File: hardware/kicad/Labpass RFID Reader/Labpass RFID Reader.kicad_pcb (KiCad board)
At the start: 2 copper layers, 74 x 74 mm, 54 parts, among them J1 Conn_01x03_Male, J2 Conn_01x04, Q1 BC517, U1 adafruit_huzzah_32, U2 LM393, U3 LM324, U4 MFRC522, Y1 27.12 MHz

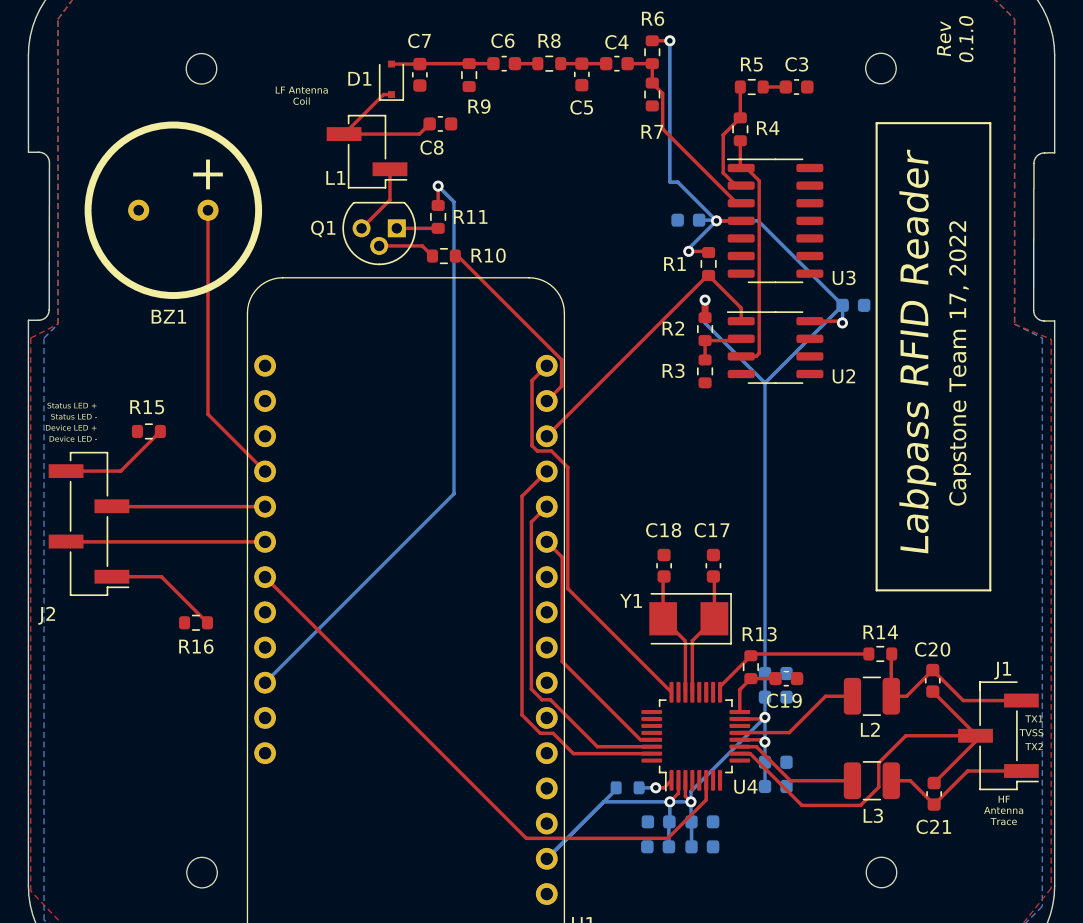
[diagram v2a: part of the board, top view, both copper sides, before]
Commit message: Add RGB LEDs with 4 wires
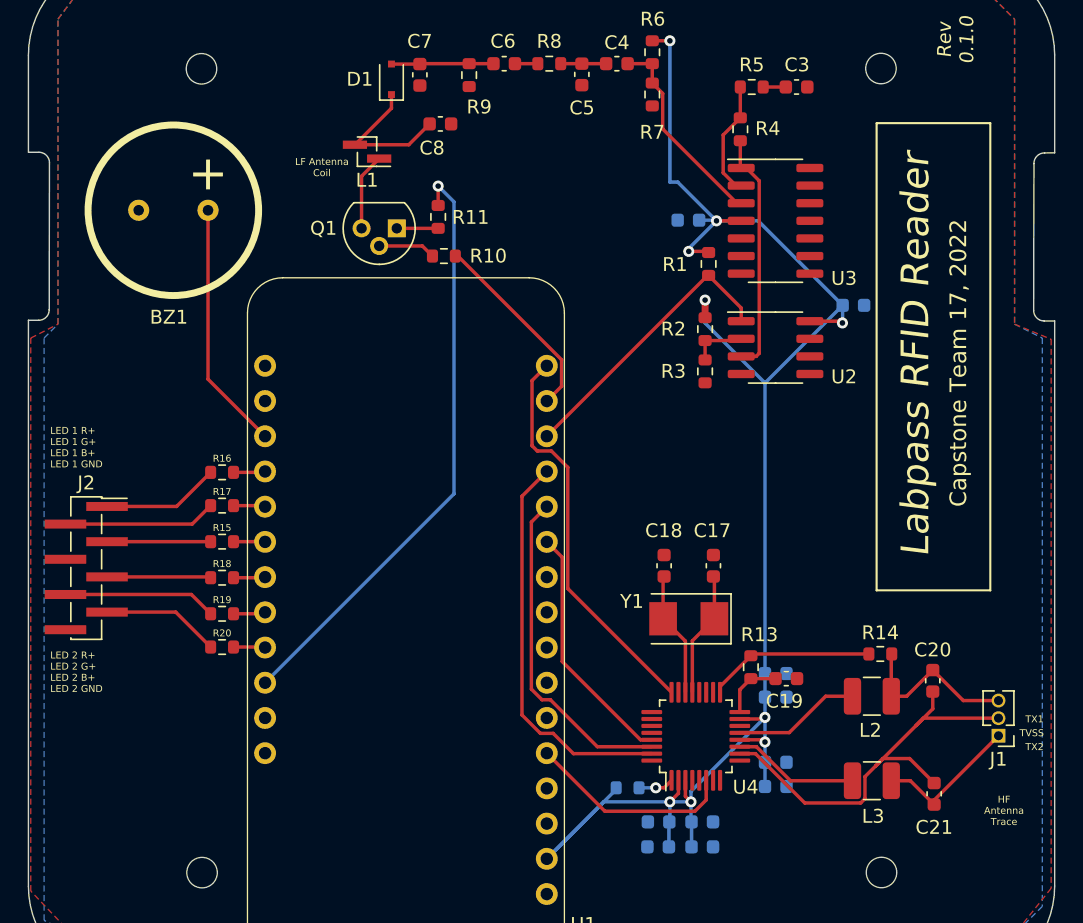
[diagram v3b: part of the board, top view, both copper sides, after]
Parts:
- added R17: R_US, Resistor_SMD:R_0603_1608Metric, F.Cu at (43.8, 70.2)
- added R18: R_US, Resistor_SMD:R_0603_1608Metric, F.Cu at (43.8, 75.4)
- added R19: R_US, Resistor_SMD:R_0603_1608Metric, F.Cu at (43.8, 78.0)
- added R20: R_US, Resistor_SMD:R_0603_1608Metric, F.Cu at (43.8, 80.4)
- J1: footprint Connector_PinHeader_2.54mm:PinHeader_1x03_P2.54mm_Vertical_SMD_Pin1Left -> Connector_PinHeader_1.27mm:PinHeader_1x03_P1.27mm_Vertical
- J2: footprint Connector_PinHeader_2.54mm:PinHeader_1x04_P2.54mm_Vertical_SMD_Pin1Left -> Connector_PinHeader_1.27mm:PinHeader_1x08_P1.27mm_Vertical_SMD_Pin1Right
- L1: footprint Connector_PinHeader_2.54mm:PinHeader_1x02_P2.54mm_Vertical_SMD_Pin1Left -> Connector_PinHeader_1.00mm:PinHeader_1x02_P1.00mm_Vertical_SMD_Pin1Left
- moved R16 11.0 mm to (43.8, 67.8)
- moved R15 9.54 mm to (43.8, 72.8)
- moved J2 3.19 mm to (34.0, 74.7), turned to 0 degrees
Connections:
- J2 pad 1: Net-(R16-Pad1) -> Net-(J2-Pad1)
- J2 pad 2: /Indicators/device_led -> Net-(J2-Pad2)
- J2 pad 3: /Indicators/status_led -> Net-(R15-Pad2)
- J2 pad 4: Net-(R15-Pad1) -> GND
- R15 pad 1: Net-(R15-Pad1) -> /Indicators/LED_1_B
- R15 pad 2: GND -> Net-(R15-Pad2)
- R16 pad 1: Net-(R16-Pad1) -> /Indicators/LED_1_R
- R16 pad 2: GND -> Net-(J2-Pad1)
- U1 pad 12: (no net) -> /Indicators/LED_2_G
- U1 pad 13: (no net) -> /Indicators/LED_2_B
- U1 pad 14: (no net) -> /Indicators/buzzer
- U1 pad 15: /Indicators/status_led -> /Indicators/LED_1_G
- U1 pad 27: /labpass_rf_13.56M/RESET -> /Indicators/LED_2_R
- U1 pad 32: /Indicators/buzzer -> /Indicators/LED_1_R
- U1 pad 33: /Indicators/device_led -> /Indicators/LED_1_B
- U1 pad A0: (no net) -> /labpass_rf_13.56M/RESET
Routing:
- net /labpass_rf_13.56M/RESET: track 42.2 -> 15.0 mm
- net /Indicators/device_led: track 14.4 -> 0.00 mm
- net /Indicators/status_led: track 11.1 -> 0.00 mm
- net Net-(J2-Pad6): track 0.00 -> 11.1 mm
- net Net-(J2-Pad2): track 0.00 -> 11.0 mm
- net Net-(J2-Pad7): track 0.00 -> 8.52 mm
- net Net-(J2-Pad1): track 0.00 -> 8.49 mm
- net Net-(R16-Pad1): track 8.26 -> 0.00 mm
- net Net-(R15-Pad1): track 7.98 -> 0.00 mm
- net Net-(J2-Pad5): track 0.00 -> 7.50 mm
- net Net-(R15-Pad2): track 0.00 -> 7.48 mm
- net /Indicators/buzzer: track 20.5 -> 18.0 mm
- net /Indicators/LED_2_G: track 0.00 -> 2.32 mm
- net /Indicators/LED_1_G: track 0.00 -> 2.31 mm
- net /Indicators/LED_1_R: track 0.00 -> 2.30 mm
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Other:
- board text added: "LED 1 R+ LED 1 G+ LED 1 B+ LED 1 GND"
- board text added: "LED 2 R+ LED 2 G+ LED 2 B+ LED 2 GND"
- board text removed: "Device LED +"
- board text removed: "Device LED -"
- board text removed: "Status LED +"
- board text removed: "Status LED -"

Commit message: last-minute fixes
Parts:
- J1: footprint Connector_PinHeader_1.27mm:PinHeader_1x03_P1.27mm_Vertical -> Connector_PinHeader_2.54mm:PinHeader_1x03_P2.54mm_Vertical_SMD_Pin1Left
- J2: footprint Connector_PinHeader_1.27mm:PinHeader_1x08_P1.27mm_Vertical_SMD_Pin1Right -> Connector_PinHeader_2.54mm:PinHeader_1x08_P2.54mm_Vertical_SMD_Pin1Right
- L1: footprint Connector_PinHeader_1.00mm:PinHeader_1x02_P1.00mm_Vertical_SMD_Pin1Left -> Connector_PinHeader_2.54mm:PinHeader_1x02_P2.54mm_Vertical_SMD_Pin1Left
- U4: footprint Package_QFP:LQFP-32_5x5mm_P0.5mm -> Package_DFN_QFN:QFN-32-1EP_5x5mm_P0.5mm_EP3.1x3.1mm
- moved J2 81.8 mm to (110.8, 102.8)
- moved J1 81.4 mm to (176.4, 114.4)
- moved C4 81.3 mm to (148.7, 65.9)
- moved R2 81.3 mm to (155.1, 85.0)
- moved R3 81.3 mm to (155.1, 88.1)
- moved R6 81.3 mm to (151.3, 65.1)
- moved R7 81.3 mm to (151.3, 68.1)
- moved BZ1 81.3 mm to (116.8, 76.5)
- moved C1 81.3 mm to (153.9, 77.2)
- moved C14 81.3 mm to (151.8, 120.6)
- moved C15 81.3 mm to (154.9, 122.4)
- moved C16 81.3 mm to (154.9, 120.6)
- moved C17 81.3 mm to (155.7, 102.1)
- moved C19 81.3 mm to (161.0, 110.2)
- moved C20 81.3 mm to (171.5, 110.4)
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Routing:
- net GND: track 0.00 -> 11.8 mm, vias 0 -> 8
- net /labpass_rf_13.56M/MISO: track 28.8 -> 32.5 mm
- net +3V3: track 126.3 -> 129.3 mm
- net Net-(C20-Pad2): track 12.5 -> 14.3 mm
- net /labpass_rf_13.56M/MOSI: track 24.0 -> 25.4 mm
- net Net-(J2-Pad7): track 8.52 -> 7.48 mm
- net Net-(J2-Pad1): track 8.49 -> 7.59 mm
- net /labpass_rf_13.56M/RX: track 12.1 -> 12.9 mm
- net /labpass_rf_13.56M/XTAL1: track 9.04 -> 9.78 mm
- net /labpass_rf_13.56M/TX1: track 9.14 -> 9.88 mm
- net /labpass_rf_13.56M/TX2: track 9.22 -> 9.96 mm
- net /labpass_rf_13.56M/SDA: track 28.8 -> 29.5 mm
- net /labpass_rf_13.56M/XTAL2: track 9.05 -> 9.79 mm
- net /labpass_rf_13.56M/SCK: track 17.9 -> 18.6 mm
- net /labpass_rf_13.56M/RESET: track 15.0 -> 15.7 mm
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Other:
- rule pad_to_mask_clearance: 0 -> 0.0508

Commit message: kicad backups
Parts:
- C19: value C -> 100n
- C20, C21: value C -> 220p
- C3: value ~ -> 100n
- J2: value Conn_01x04 -> Conn_01x08
- J3: renamed from L1; value 162u -> Conn_01x02
- L2, L3: value L -> 560n
- R13, R15, R16, R17, R18, R19, R20: value R_US -> 1k
- R14: value R_US -> 820
- R3: value 120k -> 110k
- R9: value 267k -> 222k
- U4: footprint Package_DFN_QFN:QFN-32-1EP_5x5mm_P0.5mm_EP3.1x3.1mm -> Package_QFP:LQFP-32_5x5mm_P0.5mm

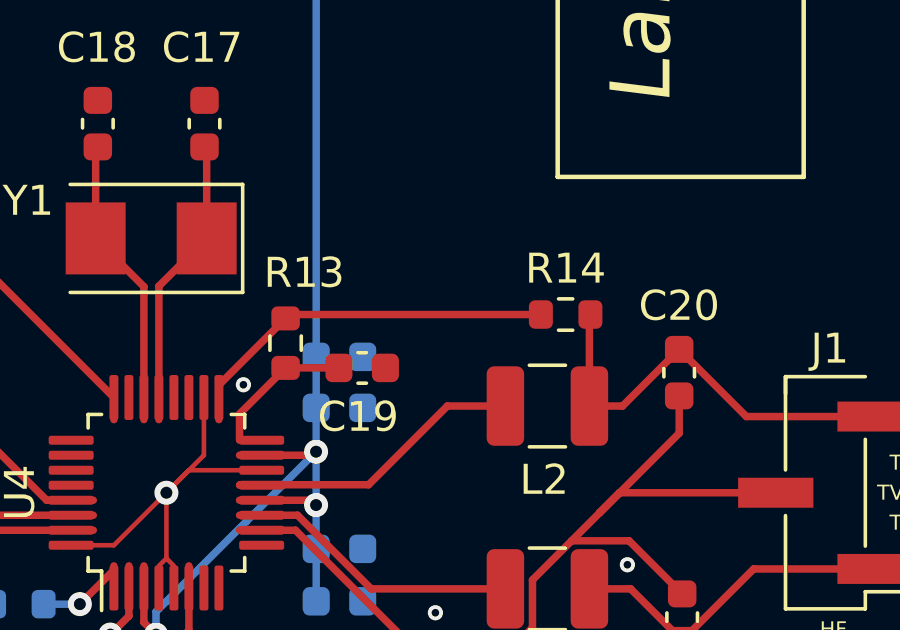
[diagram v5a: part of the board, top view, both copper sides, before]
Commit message: add missing dc blocking cap to HF path
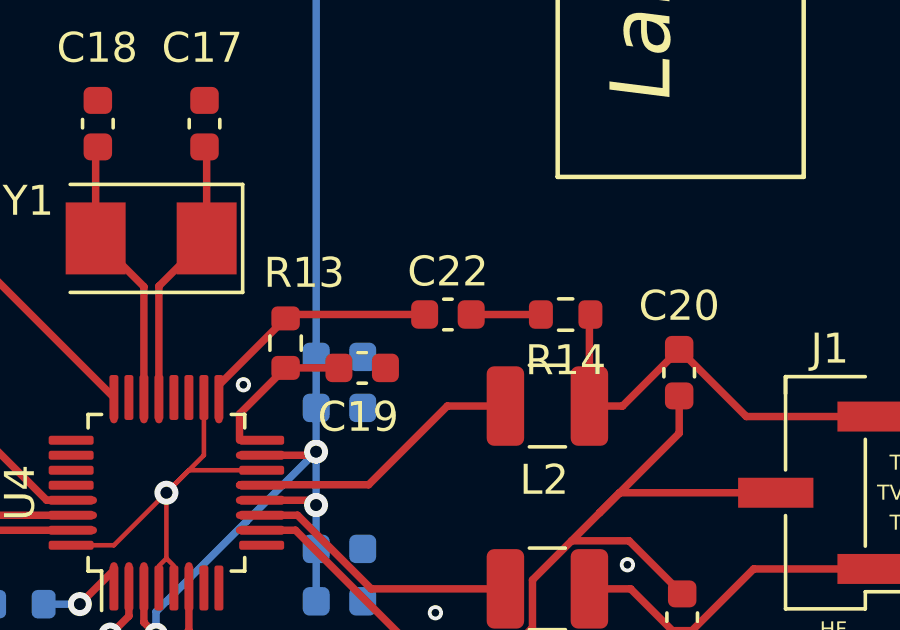
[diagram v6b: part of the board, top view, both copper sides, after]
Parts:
- added C22: 1n, Capacitor_SMD:C_0603_1608Metric, F.Cu at (163.8, 108.5)
- turned R14 to 180 degrees
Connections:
- C20 pad 2: Net-(C20-Pad2) -> Net-(R14-Pad1)
- J1 pad 3: Net-(C20-Pad2) -> Net-(R14-Pad1)
- L2 pad 2: Net-(C20-Pad2) -> Net-(R14-Pad1)
- R14 pad 1: /labpass_rf_13.56M/RX -> Net-(R14-Pad1)
- R14 pad 2: Net-(C20-Pad2) -> Net-(R14-Pad2)
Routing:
- net Net-(R14-Pad1): track 0.00 -> 14.3 mm
- net Net-(C20-Pad2): track 14.3 -> 0.00 mm
- net /labpass_rf_13.56M/RX: track 12.9 -> 8.99 mm
- net Net-(R14-Pad2): track 0.00 -> 2.33 mm
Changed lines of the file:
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@@
   (net 7 "Net-(C6-Pad2)")
   (net 8 "Net-(C8-Pad1)")
-  (net 9 "Net-(C20-Pad2)")
+  (net 9 "Net-(R14-Pad1)")
   (net 10 "Net-(C21-Pad1)")
-  (net 11 "Net-(Q1-Pad3)")
+  (net 11 "Net-(R14-Pad2)")
   (net 12 "Net-(Q1-Pad1)")
   (net 13 "Net-(Q1-Pad2)")
@@
   (net 44 "/Indicators/LED_2_B")
   (net 45 "Net-(J2-Pad3)")
+  (net 46 "Net-(J3-Pad1)")
   (footprint "Resistor_SMD:R_0603_1608Metric" (layer "F.Cu")
     (at 120.266182 100.36028 180)
@@
       (net 30 "/labpass_rf_13.56M/TX2") (pinfunction "1") (pintype "passive"))
     (pad "2" smd roundrect (at 1.4 0) (size 1.25 2.65) (layers "F.Cu" "F.Paste" "F.Mask") (roundrect_rratio 0.2)
-      (net 9 "Net-(C20-Pad2)") (pinfunction "2") (pintype "passive"))
+      (net 9 "Net-(R14-Pad1)") (pinfunction "2") (pintype "passive"))
     (model "${KICAD6_3DMODEL_DIR}/Inductor_SMD.3dshapes/L_1210_3225Metric.wrl"
       (offset (xyz 0 0 0))
@@
     (fp_line (start 1.27 -2.54) (end 1.27 2.54) (layer "F.Fab") (width 0.1))
     (pad "1" smd rect (at -1.655 -1.27 180) (size 2.51 1) (layers "F.Cu" "F.Paste" "F.Mask")
-      (net 11 "Net-(Q1-Pad3)") (pinfunction "Pin_1") (pintype "passive"))
+      (net 46 "Net-(J3-Pad1)") (pinfunction "Pin_1") (pintype "passive"))
     (pad "2" smd rect (at 1.655 1.27 180) (size 2.51 1) (layers "F.Cu" "F.Paste" "F.Mask")
       (net 8 "Net-(C8-Pad1)") (pinfunction "Pin_2") (pintype "passive"))
@@
   )
   (footprint "Resistor_SMD:R_0603_1608Metric" (layer "F.Cu")
-    (at 167.741169 108.460169)
+    (at 167.741169 108.460169 180)
     (descr "Resistor SMD 0603 (1608 Metric), square (rectangular) end terminal, IPC_7351 nominal, (Body size source: IPC-SM-782 page 72, https://www.pcb-3d.com/wordpress/wp-content/uploads/ipc-sm-782a_amendment_1_and_2.pdf), generated with kicad-footprint-generator")
     (tags "resistor")
@@
       (effects (font (size 1 1) (thickness 0.15)))
     )
-    (fp_text value "820" (at 0 -1.780169) (layer "F.Fab")
+    (fp_text value "820" (at 0 1.526169) (layer "F.Fab")
       (effects (font (size 1 1) (thickness 0.15)))
     )
@@
     (fp_line (start 0.8 -0.4125) (end 0.8 0.4125) (layer "F.Fab") (width 0.1))
     (fp_line (start -0.8 -0.4125) (end 0.8 -0.4125) (layer "F.Fab") (width 0.1))
-    (pad "1" smd roundrect (at -0.825 0) (size 0.8 0.95) (layers "F.Cu" "F.Paste" "F.Mask") (roundrect_rratio 0.25)
-      (net 32 "/labpass_rf_13.56M/RX") (pintype "passive"))
-    (pad "2" smd roundrect (at 0.825 0) (size 0.8 0.95) (layers "F.Cu" "F.Paste" "F.Mask") (roundrect_rratio 0.25)
-      (net 9 "Net-(C20-Pad2)") (pintype "passive"))
+    (pad "1" smd roundrect (at -0.825 0 180) (size 0.8 0.95) (layers "F.Cu" "F.Paste" "F.Mask") (roundrect_rratio 0.25)
+      (net 9 "Net-(R14-Pad1)") (pintype "passive"))
+    (pad "2" smd roundrect (at 0.825 0 180) (size 0.8 0.95) (layers "F.Cu" "F.Paste" "F.Mask") (roundrect_rratio 0.25)
+      (net 11 "Net-(R14-Pad2)") (pintype "passive"))
     (model "${KICAD6_3DMODEL_DIR}/Resistor_SMD.3dshapes/R_0603_1608Metric.wrl"
       (offset (xyz 0 0 0))
@@
       (net 13 "Net-(Q1-Pad2)") (pinfunction "B") (pintype "input"))
     (pad "3" thru_hole circle (at 2.54 0 180) (size 1.3 1.3) (drill 0.75) (layers *.Cu *.Mask)
-      (net 11 "Net-(Q1-Pad3)") (pinfunction "E") (pintype "passive"))
+      (net 46 "Net-(J3-Pad1)") (pinfunction "E") (pintype "passive"))
     (model "${KICAD6_3DMODEL_DIR}/Package_TO_SOT_THT.3dshapes/TO-92.wrl"
       (offset (xyz 0 0 0))
@@
       (net 29 "/labpass_rf_13.56M/TVSS") (pinfunction "Pin_2") (pintype "passive"))
     (pad "3" smd rect (at -1.655 2.54 180) (size 2.51 1) (layers "F.Cu" "F.Paste" "F.Mask")
-      (net 9 "Net-(C20-Pad2)") (pinfunction "Pin_3") (pintype "passive"))
+      (net 9 "Net-(R14-Pad1)") (pinfunction "Pin_3") (pintype "passive"))
     (model "${KICAD6_3DMODEL_DIR}/Connector_PinHeader_2.54mm.3dshapes/PinHeader_1x03_P2.54mm_Vertical_SMD_Pin1Left.wrl"
       (offset (xyz 0 0 0))
@@
       (net 29 "/labpass_rf_13.56M/TVSS") (pintype "passive"))
     (pad "2" smd roundrect (at 0.775 0 90) (size 0.9 0.95) (layers "F.Cu" "F.Paste" "F.Mask") (roundrect_rratio 0.25)
-      (net 9 "Net-(C20-Pad2)") (pintype "passive"))
+      (net 9 "Net-(R14-Pad1)") (pintype "passive"))
+    (model "${KICAD6_3DMODEL_DIR}/Capacitor_SMD.3dshapes/C_0603_1608Metric.wrl"
+      (offset (xyz 0 0 0))
+      (scale (xyz 1 1 1))
+      (rotate (xyz 0 0 0))
+    )
+  )
+  (footprint "Capacitor_SMD:C_0603_1608Metric" (layer "F.Cu")
+    (at 163.817 108.458)
+    (descr "Capacitor SMD 0603 (1608 Metric), square (rectangular) end terminal, IPC_7351 nominal, (Body size source: IPC-SM-782 page 76, https://www.pcb-3d.com/wordpress/wp-content/uploads/ipc-sm-782a_amendment_1_and_2.pdf), generated with kicad-footprint-generator")
+    (tags "capacitor")
+    (property "Sheetfile" "HF_RF.kicad_sch")
+    (property "Sheetname" "labpass_rf_13.56M")
+    (attr smd)
+    (fp_text reference "C22" (at 0 -1.43) (layer "F.SilkS")
+      (effects (font (size 1 1) (thickness 0.15)))
+    )
+    (fp_text value "1n" (at 0 1.43) (layer "F.Fab")
+      (effects (font (size 1 1) (thickness 0.15)))
+    )
+    (fp_text user "${REFERENCE}" (at 0 0) (layer "F.Fab")
+      (effects (font (size 0.4 0.4) (thickness 0.06)))
+    )
+    (fp_line (start -0.14058 0.51) (end 0.14058 0.51) (layer "F.SilkS") (width 0.12))
+    (fp_line (start -0.14058 -0.51) (end 0.14058 -0.51) (layer "F.SilkS") (width 0.12))
+    (fp_line (start -1.48 -0.73) (end 1.48 -0.73) (layer "F.CrtYd") (width 0.05))
+    (fp_line (start 1.48 -0.73) (end 1.48 0.73) (layer "F.CrtYd") (width 0.05))
+    (fp_line (start 1.48 0.73) (end -1.48 0.73) (layer "F.CrtYd") (width 0.05))
+    (fp_line (start -1.48 0.73) (end -1.48 -0.73) (layer "F.CrtYd") (width 0.05))
+    (fp_line (start -0.8 -0.4) (end 0.8 -0.4) (layer "F.Fab") (width 0.1))
+    (fp_line (start 0.8 0.4) (end -0.8 0.4) (layer "F.Fab") (width 0.1))
+    (fp_line (start 0.8 -0.4) (end 0.8 0.4) (layer "F.Fab") (width 0.1))
+    (fp_line (start -0.8 0.4) (end -0.8 -0.4) (layer "F.Fab") (width 0.1))
+    (pad "1" smd roundrect (at -0.775 0) (size 0.9 0.95) (layers "F.Cu" "F.Paste" "F.Mask") (roundrect_rratio 0.25)
+      (net 32 "/labpass_rf_13.56M/RX") (pintype "passive"))
+    (pad "2" smd roundrect (at 0.775 0) (size 0.9 0.95) (layers "F.Cu" "F.Paste" "F.Mask") (roundrect_rratio 0.25)
+      (net 11 "Net-(R14-Pad2)") (pintype "passive"))
     (model "${KICAD6_3DMODEL_DIR}/Capacitor_SMD.3dshapes/C_0603_1608Metric.wrl"
       (offset (xyz 0 0 0))
@@
   (segment (start 169.908169 117.604169) (end 171.626169 119.322169) (width 0.25) (layer "F.Cu") (net 10))
   (segment (start 174.008338 116.94) (end 178.055 116.94) (width 0.25) (layer "F.Cu") (net 10))
-  (segment (start 132.055 73.07) (end 132.055 76.031462) (width 0.25) (layer "F.Cu") (net 11))
-  (segment (start 132.055 76.031462) (end 130.326182 77.76028) (width 0.25) (layer "F.Cu") (net 11))
+  (segment (start 164.594169 108.460169) (end 164.592 108.458) (width 0.25) (layer "F.Cu") (net 11))
+  (segment (start 166.916169 108.460169) (end 164.594169 108.460169) (width 0.25) (layer "F.Cu") (net 11))
   (segment (start 132.866182 77.76028) (end 135.851182 77.76028) (width 0.25) (layer "F.Cu") (net 12))
   (segment (start 131.596182 79.03028) (end 134.711182 79.03028) (width 0.25) (layer "F.Cu") (net 13))
@@
   (segment (start 161.258871 117.604169) (end 165.733169 117.604169) (width 0.25) (layer "F.Cu") (net 31))
   (segment (start 156.183169 111.962669) (end 156.183169 110.811169) (width 0.25) (layer "F.Cu") (net 32))
-  (segment (start 158.534169 108.460169) (end 158.406169 108.588169) (width 0.25) (layer "F.Cu") (net 32))
+  (segment (start 163.042 108.458) (end 158.536338 108.458) (width 0.25) (layer "F.Cu") (net 32))
   (segment (start 156.183169 110.811169) (end 158.406169 108.588169) (width 0.25) (layer "F.Cu") (net 32))
-  (segment (start 166.916169 108.460169) (end 158.534169 108.460169) (width 0.25) (layer "F.Cu") (net 32))
+  (segment (start 158.536338 108.458) (end 158.406169 108.588169) (width 0.25) (layer "F.Cu") (net 32))
   (segment (start 117.990902 93.91) (end 119.441182 95.36028) (width 0.25) (layer "F.Cu") (net 33))
   (segment (start 112.455 93.91) (end 117.990902 93.91) (width 0.25) (layer "F.Cu") (net 33))
@@
   (segment (start 118.070902 98.99) (end 119.441182 100.36028) (width 0.25) (layer "F.Cu") (net 45))
   (segment (start 112.455 98.99) (end 118.070902 98.99) (width 0.25) (layer "F.Cu") (net 45))
+  (segment (start 132.055 73.07) (end 132.055 76.031462) (width 0.25) (layer "F.Cu") (net 46))
+  (segment (start 132.055 76.031462) (end 130.326182 77.76028) (width 0.25) (layer "F.Cu") (net 46))
   (zone locked (net 2) (net_name "GND") (layer "F.Cu") (hatch edge 0.508)
     (connect_pads (clearance 0))
